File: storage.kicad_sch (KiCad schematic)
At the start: 9 parts, among them J4 503398-1892, J5 2171840001

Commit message: pcb / inital work
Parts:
- removed D3: D_Generic, symbol PCM_4ms_Diode:D_Generic
- added D3: SS14, PCM_Diode_SMD_AKL:D_SMA, symbol PCM_Diode_Schottky_AKL:SS14
- C22: footprint Capacitor_THT:C_Disc_D3.0mm_W2.0mm_P2.50mm -> Capacitor_SMD:C_0805_2012Metric
- FB2: value FerriteBead -> 220@100MHz; footprint (none) -> PCM_Ferrite_SMD_AKL:Ferrite_0603_1608Metric
- J4: footprint 503398-1892:MOLEX_503398-1892 -> uwu:MOLEX_503398-1892
- J5: footprint 2171840001:MOLEX_2171840001 -> uwu:MOLEX_2171840001
- R16, R17, R36: footprint (none) -> Resistor_SMD:R_0603_1608Metric
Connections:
- net USB_VBUS: now also D3.2 (A)
- net at C22.2, FB2.1: now also D3.1 (K)

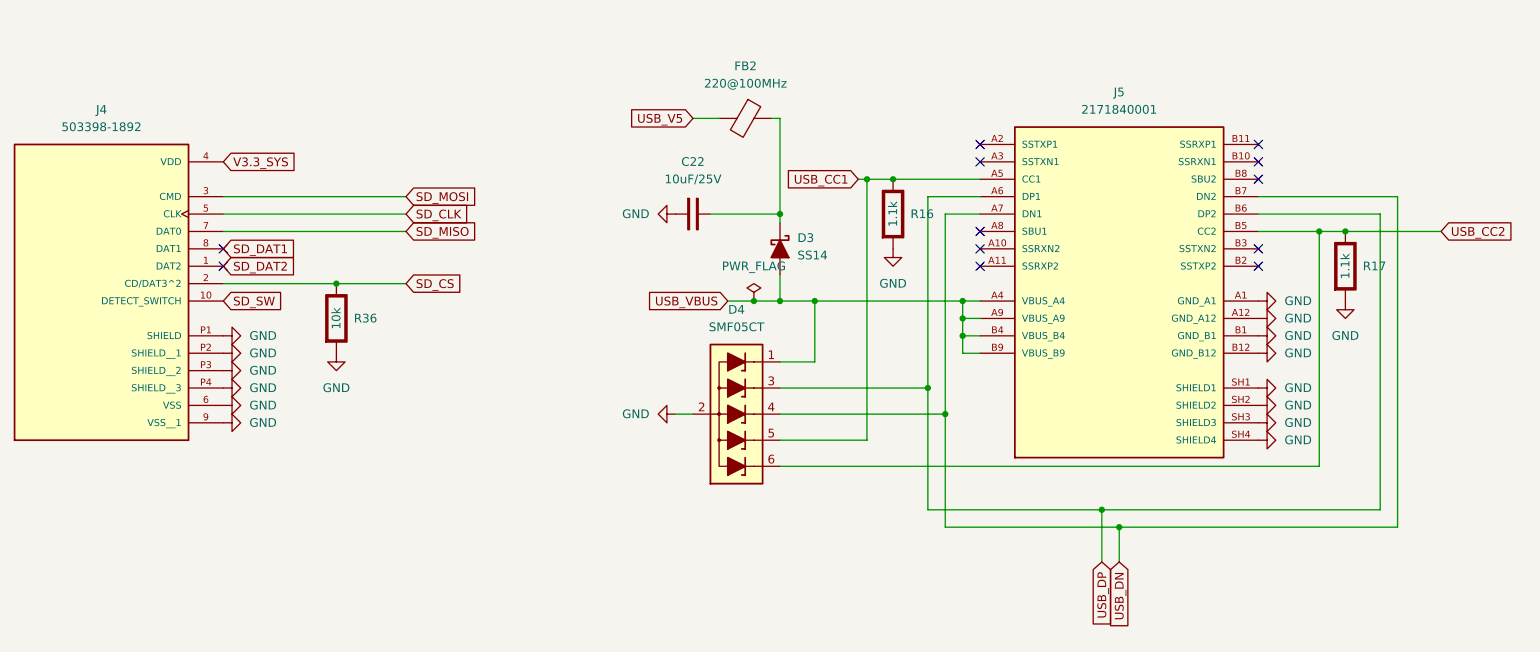
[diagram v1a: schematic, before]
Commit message: ICs placed
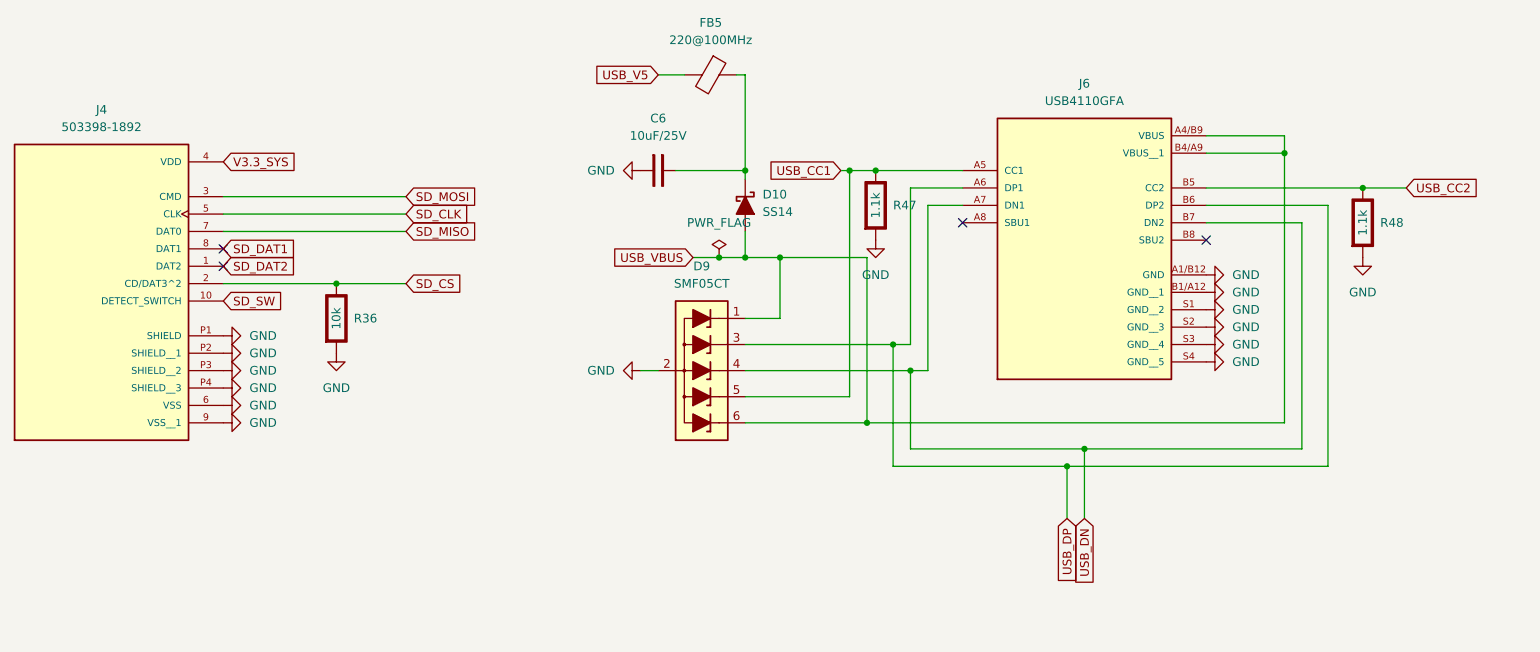
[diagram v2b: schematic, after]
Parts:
- removed C22: 10uF/25V, Capacitor_SMD:C_0805_2012Metric, symbol PCM_SL_Devices:Capacitor_NP
- removed D3: SS14, PCM_Diode_SMD_AKL:D_SMA, symbol PCM_Diode_Schottky_AKL:SS14
- removed D4: SMF05CT, PCM_Package_TO_SOT_SMD_AKL:SOT-363_SC-70-6, symbol PCM_Diode_TVS_AKL:SMF05CT
- removed FB2: 220@100MHz, PCM_Ferrite_SMD_AKL:Ferrite_0603_1608Metric, symbol Device:FerriteBead
- removed J5: 2171840001, uwu:MOLEX_2171840001, symbol uwu:2171840001
- removed R16, R17: 1.1k, Resistor_SMD:R_0603_1608Metric, symbol PCM_Elektuur:R
- added C6: 10uF/25V, Capacitor_SMD:C_0805_2012Metric, symbol PCM_SL_Devices:Capacitor_NP
- added D10: SS14, PCM_Diode_SMD_AKL:D_SMA, symbol PCM_Diode_Schottky_AKL:SS14
- added D9: SMF05CT, PCM_Package_TO_SOT_SMD_AKL:SOT-363_SC-70-6, symbol PCM_Diode_TVS_AKL:SMF05CT
- added FB5: 220@100MHz, PCM_Ferrite_SMD_AKL:Ferrite_0603_1608Metric, symbol Device:FerriteBead
- added J6: USB4110GFA, uwu:GCT_USB4110GFA, symbol uwu:USB4110GFA
- added R47, R48: 1.1k, Resistor_SMD:R_0603_1608Metric, symbol PCM_Elektuur:R
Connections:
- net GND: now also C6.1, D9.2 (VN), J6.A1/B12 (GND), J6.B1/A12 (GND__1), J6.S1 (GND__2), J6.S2 (GND__3), J6.S3 (GND__4), J6.S4 (GND__5), R47.2 (-), R48.2 (-)
- net USB_CC1: now also D9.5 (L4), J6.A5 (CC1), R47.1 (+)
- net USB_CC2: now also J6.B5 (CC2), R48.1 (+)
- net USB_DN: now also D9.4 (L3), J6.A7 (DN1), J6.B7 (DN2)
- net USB_DP: now also D9.3 (L2), J6.A6 (DP1), J6.B6 (DP2)
- net USB_V5: now also FB5.2
- net USB_VBUS: now also D10.2 (A), D9.1 (L1), D9.6 (L5), J6.A4/B9 (VBUS), J6.B4/A9 (VBUS__1)
- new net: C6.2, D10.1 (K), FB5.1
- no-connect marks 12 -> 4
